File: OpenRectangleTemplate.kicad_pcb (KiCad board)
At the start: 2 copper layers, 38.1 x 49.2 mm, 40 parts, among them J1 USB C Connector, J2 JTAG_TC2030, SW1 Boot, U1 XC6206, U2 USBLC6-2SC6, U3 RP2040, U4 W25Q128JVS, Y1 12MHz

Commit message: Prototyped and tested
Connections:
- U3 pad 2: unconnected-(U3-GPIO0-Pad2) -> START
- U3 pad 3: START -> unconnected-(U3-GPIO1-Pad3)
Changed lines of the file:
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@@
   (net 34 "CS")
   (net 35 "XTAL_OUT")
-  (net 36 "unconnected-(U3-GPIO0-Pad2)")
+  (net 36 "unconnected-(U3-GPIO1-Pad3)")
   (net 37 "START")
   (net 38 "RIGHT")
@@
       (net 2 "+3V3") (pinfunction "IOVDD") (pintype "power_in"))
     (pad "2" smd roundrect (at -3.4375 -2.2) (size 0.875 0.2) (layers "F.Cu" "F.Paste" "F.Mask") (roundrect_rratio 0.25)
-      (net 36 "unconnected-(U3-GPIO0-Pad2)") (pinfunction "GPIO0") (pintype "input"))
+      (net 37 "START") (pinfunction "GPIO0") (pintype "input"))
     (pad "3" smd roundrect (at -3.4375 -1.8) (size 0.875 0.2) (layers "F.Cu" "F.Paste" "F.Mask") (roundrect_rratio 0.25)
-      (net 37 "START") (pinfunction "GPIO1") (pintype "input"))
+      (net 36 "unconnected-(U3-GPIO1-Pad3)") (pinfunction "GPIO1") (pintype "input"))
     (pad "4" smd roundrect (at -3.4375 -1.4) (size 0.875 0.2) (layers "F.Cu" "F.Paste" "F.Mask") (roundrect_rratio 0.25)
       (net 38 "RIGHT") (pinfunction "GPIO2") (pintype "input"))
@@
   (arc (start 139.213089 57.718603) (mid 139.235925 57.603798) (end 139.300957 57.506471) (width 0.2) (layer "F.Cu") (net 35))
   (segment (start 127.514615 55.73973) (end 127.514615 59.64) (width 0.2) (layer "F.Cu") (net 37))
-  (segment (start 132.442676 49.943816) (end 128.128276 54.258221) (width 0.2) (layer "F.Cu") (net 37))
-  (segment (start 136.918589 49.031089) (end 134.646194 49.031089) (width 0.2) (layer "F.Cu") (net 37))
+  (segment (start 132.153246 50.233246) (end 128.128276 54.258221) (width 0.2) (layer "F.Cu") (net 37))
+  (segment (start 136.918589 48.631089) (end 135.970519 48.631089) (width 0.2) (layer "F.Cu") (net 37))
+  (segment (start 132.189081 50.197411) (end 132.153246 50.233246) (width 0.2) (layer "F.Cu") (net 37))
+  (arc (start 135.970519 48.631089) (mid 133.92402 49.038163) (end 132.189081 50.197411) (width 0.2) (layer "F.Cu") (net 37))
   (arc (start 128.128276 54.258221) (mid 127.674101 54.937943) (end 127.514615 55.73973) (width 0.2) (layer "F.Cu") (net 37))
-  (arc (start 134.646194 49.031089) (mid 133.453659 49.268299) (end 132.442676 49.943816) (width 0.2) (layer "F.Cu") (net 37))
   (segment (start 134.76373 49.431089) (end 136.918589 49.431089) (width 0.2) (layer "F.Cu") (net 38))
   (segment (start 127.914615 55.941589) (end 127.914615 60.07) (width 0.2) (layer "F.Cu") (net 38))

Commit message: Adjusted part numbers
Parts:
- R4: value 470 -> 10k
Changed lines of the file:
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@@
     (property "ki_description" "Push button switch, generic, two pins")
     (property "ki_keywords" "switch normally-open pushbutton push-button")
-    (attr smd exclude_from_bom)
+    (attr smd)
     (fp_text reference "SW1" (at 0 -3.6 90) (layer "F.SilkS") hide
         (effects (font (size 1 1) (thickness 0.15)))
@@
     (property "ki_description" "6-pin TC2030 connector for JTAG programming")
     (property "ki_keywords" "JTAG ARM SWD connector tag connect tc 2030")
-    (attr exclude_from_pos_files)
+    (attr exclude_from_pos_files exclude_from_bom)
     (fp_text reference "J2" (at 0 2.7 90) (layer "F.SilkS")
         (effects (font (size 0.6 0.6) (thickness 0.15)))
@@
         (effects (font (size 0.6 0.6) (thickness 0.15)))
     )
-    (fp_text value "470" (at 0 1.17) (layer "F.Fab")
-        (effects (font (size 1 1) (thickness 0.15)))
-    )
+    (fp_text value "10k" (at 0 1.17) (layer "F.Fab")
+        (effects (font (size 1 1) (thickness 0.15)))
+    )

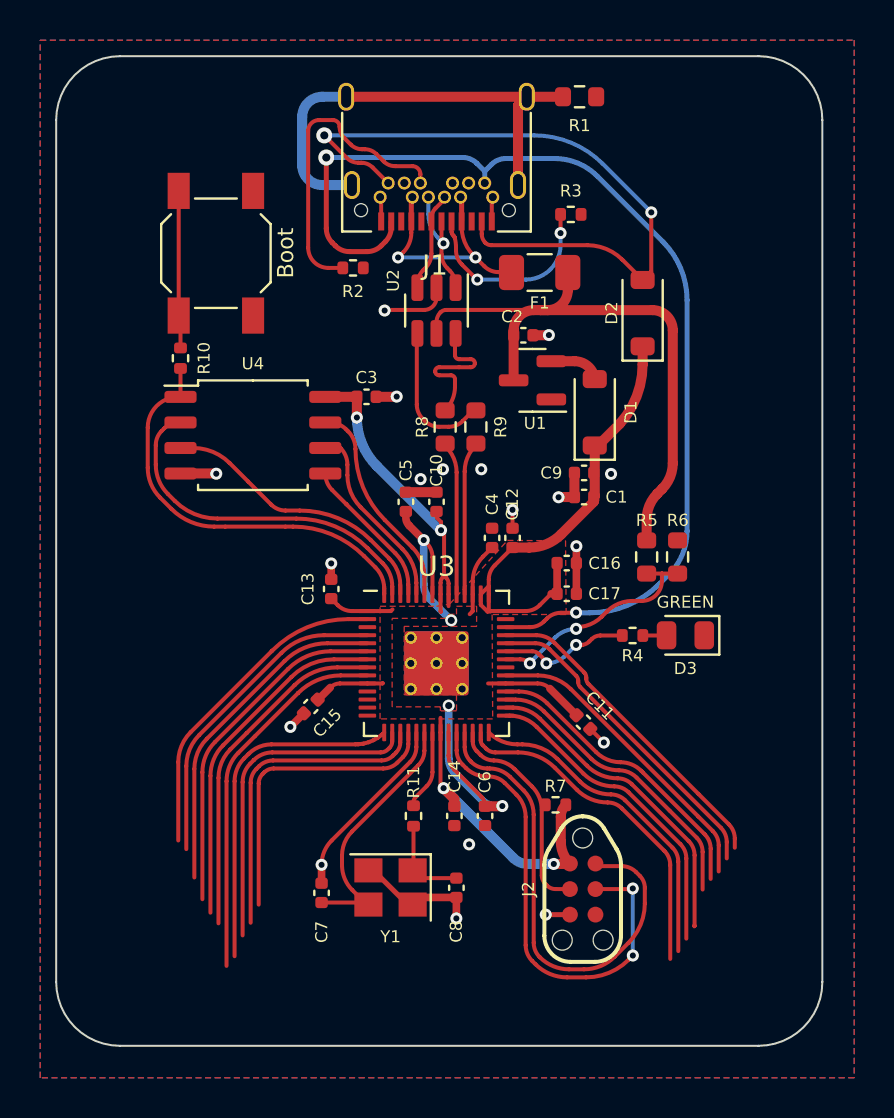
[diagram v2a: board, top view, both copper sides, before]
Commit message: Updated 3D models and footprints
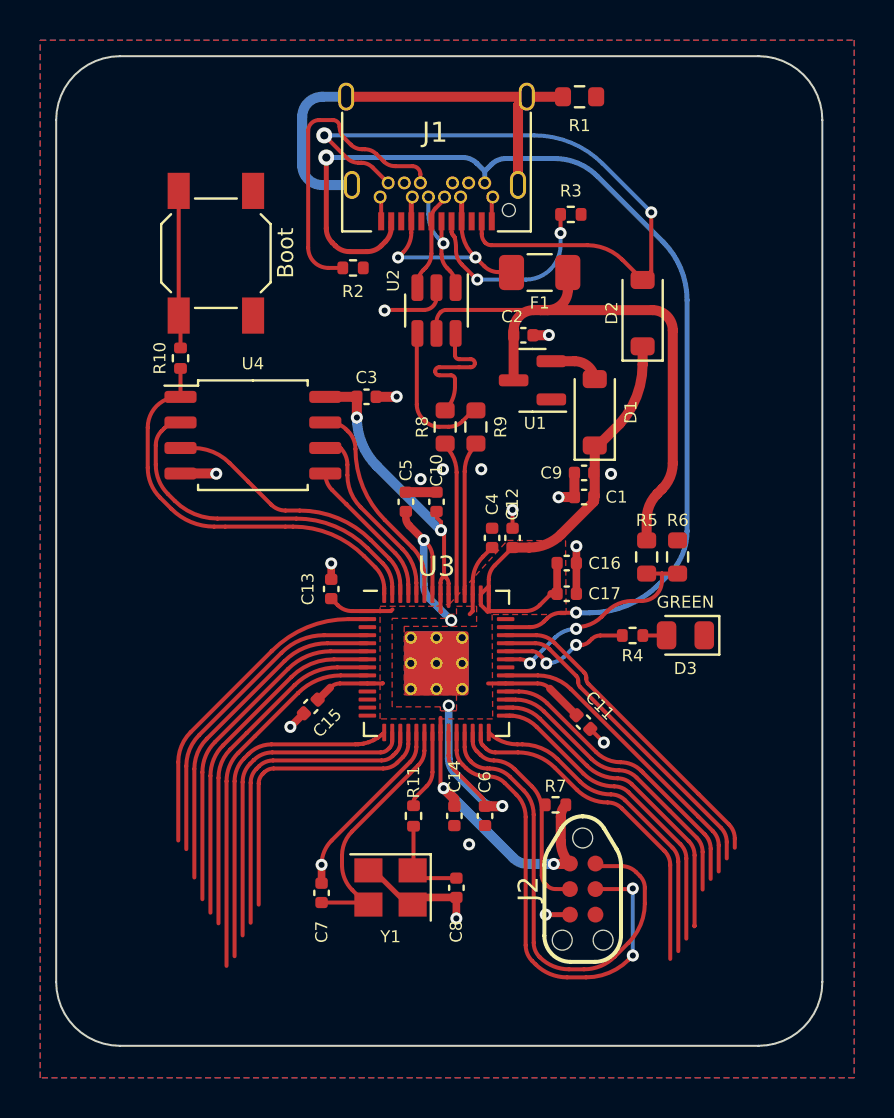
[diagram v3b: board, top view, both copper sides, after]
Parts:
- J2: footprint marbastlib-various:CON_TC2030_outlined -> PCM_marbastlib-various:CON_TC2030_outlined
- R4: value 10k -> 470
- moved J1 3.11 mm to (140.4, 20.8)

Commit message: Actually a template now
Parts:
- R4: value 470 -> 10k
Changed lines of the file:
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@@
     (descr "Resistor SMD 0603 (1608 Metric), square (rectangular) end terminal, IPC_7351 nominal, (Body size source: IPC-SM-782 page 72, https://www.pcb-3d.com/wordpress/wp-content/uploads/ipc-sm-782a_amendment_1_and_2.pdf), generated with kicad-footprint-generator")
     (tags "resistor")
-    (property "LCSC" "C23192")
+    (property "LCSC" "C25804")
     (property "Sheetfile" "OpenRectangleTemplate.kicad_sch")
     (property "Sheetname" "")
@@
     (property "Sheetfile" "OpenRectangleTemplate.kicad_sch")
     (property "Sheetname" "")
-    (property "exclude_from_bom" "")
     (property "ki_description" "Push button switch, generic, two pins")
     (property "ki_keywords" "switch normally-open pushbutton push-button")
-    (attr smd exclude_from_bom)
+    (attr smd)
     (fp_text reference "SW1" (at 0 -3.6 90) (layer "F.SilkS") hide
         (effects (font (size 1 1) (thickness 0.15)))
@@
     (fp_line (start 3.5 3.5) (end -3.5 3.5)
       (stroke (width 0.1) (type solid)) (layer "F.Fab"))
-    (pad "" smd roundrect (at -0.6375 -0.6375) (size 1.084435 1.084435) (layers "F.Paste") (roundrect_rratio 0.230535))
-    (pad "" smd roundrect (at -0.6375 0.6375) (size 1.084435 1.084435) (layers "F.Paste") (roundrect_rratio 0.230535))
-    (pad "" smd roundrect (at 0.6375 -0.6375) (size 1.084435 1.084435) (layers "F.Paste") (roundrect_rratio 0.230535))
-    (pad "" smd roundrect (at 0.6375 0.6375) (size 1.084435 1.084435) (layers "F.Paste") (roundrect_rratio 0.230535))
+    (pad "" smd roundrect (at -0.6375 -0.6375) (size 1.084435 1.084435) (layers "F.Paste") (roundrect_rratio 0.2305347946))
+    (pad "" smd roundrect (at -0.6375 0.6375) (size 1.084435 1.084435) (layers "F.Paste") (roundrect_rratio 0.2305347946))
+    (pad "" smd roundrect (at 0.6375 -0.6375) (size 1.084435 1.084435) (layers "F.Paste") (roundrect_rratio 0.2305347946))
+    (pad "" smd roundrect (at 0.6375 0.6375) (size 1.084435 1.084435) (layers "F.Paste") (roundrect_rratio 0.2305347946))
     (pad "1" smd roundrect (at -3.4375 -2.6) (size 0.875 0.2) (layers "F.Cu" "F.Paste" "F.Mask") (roundrect_rratio 0.25)
       (net 2 "+3V3") (pinfunction "IOVDD") (pintype "power_in"))
@@
     (descr "Resistor SMD 0402 (1005 Metric), square (rectangular) end terminal, IPC_7351 nominal, (Body size source: IPC-SM-782 page 72, https://www.pcb-3d.com/wordpress/wp-content/uploads/ipc-sm-782a_amendment_1_and_2.pdf), generated with kicad-footprint-generator")
     (tags "resistor")
-    (property "LCSC" "C25744")
+    (property "LCSC" "C25905")
     (property "Sheetfile" "OpenRectangleTemplate.kicad_sch")
     (property "Sheetname" "")
@@
     (descr "Resistor SMD 0402 (1005 Metric), square (rectangular) end terminal, IPC_7351 nominal, (Body size source: IPC-SM-782 page 72, https://www.pcb-3d.com/wordpress/wp-content/uploads/ipc-sm-782a_amendment_1_and_2.pdf), generated with kicad-footprint-generator")
     (tags "resistor")
-    (property "LCSC" "C25744")
+    (property "LCSC" "C25905")
     (property "Sheetfile" "OpenRectangleTemplate.kicad_sch")
     (property "Sheetname" "")
@@
     (property "Sheetfile" "OpenRectangleTemplate.kicad_sch")
     (property "Sheetname" "")
+    (property "exclude_from_bom" "")
     (property "ki_description" "6-pin TC2030 connector for JTAG programming")
     (property "ki_keywords" "JTAG ARM SWD connector tag connect tc 2030")
-    (attr exclude_from_pos_files)
-    (fp_text reference "J2" (at 0 2.7 -90) (layer "F.SilkS")
-        (effects (font (size 1 1) (thickness 0.15)))
-    )
-    (fp_text value "JTAG_TC2030" (at 0 -2.3 -90) (layer "F.Fab")
-        (effects (font (size 1 1) (thickness 0.15)))
-    )
-    (fp_text user "KEEPOUT" (at 0 0 -90) (layer "Cmts.User")
+    (attr exclude_from_pos_files exclude_from_bom)
+    (fp_text reference "J2" (at 0 2.7 90) (layer "F.SilkS")
+        (effects (font (size 1 1) (thickness 0.15)))
+    )
+    (fp_text value "JTAG_TC2030" (at 0 -2.3 90) (layer "F.Fab")
+        (effects (font (size 1 1) (thickness 0.15)))
+    )
+    (fp_text user "KEEPOUT" (at 0 0 90) (layer "Cmts.User")
         (effects (font (size 0.4 0.4) (thickness 0.07)))
     )
@@
     (descr "Resistor SMD 0603 (1608 Metric), square (rectangular) end terminal, IPC_7351 nominal, (Body size source: IPC-SM-782 page 72, https://www.pcb-3d.com/wordpress/wp-content/uploads/ipc-sm-782a_amendment_1_and_2.pdf), generated with kicad-footprint-generator")
     (tags "resistor")
-    (property "LCSC" "C25190")
+    (property "LCSC" "C22935")
     (property "Sheetfile" "OpenRectangleTemplate.kicad_sch")
     (property "Sheetname" "")
@@
         (effects (font (size 0.6 0.6) (thickness 0.15)))
     )
-    (fp_text value "470" (at 0 1.17) (layer "F.Fab")
-        (effects (font (size 1 1) (thickness 0.15)))
-    )
+    (fp_text value "10k" (at 0 1.17) (layer "F.Fab")
+        (effects (font (size 1 1) (thickness 0.15)))
+    )
